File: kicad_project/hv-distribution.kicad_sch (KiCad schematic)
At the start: 33 parts

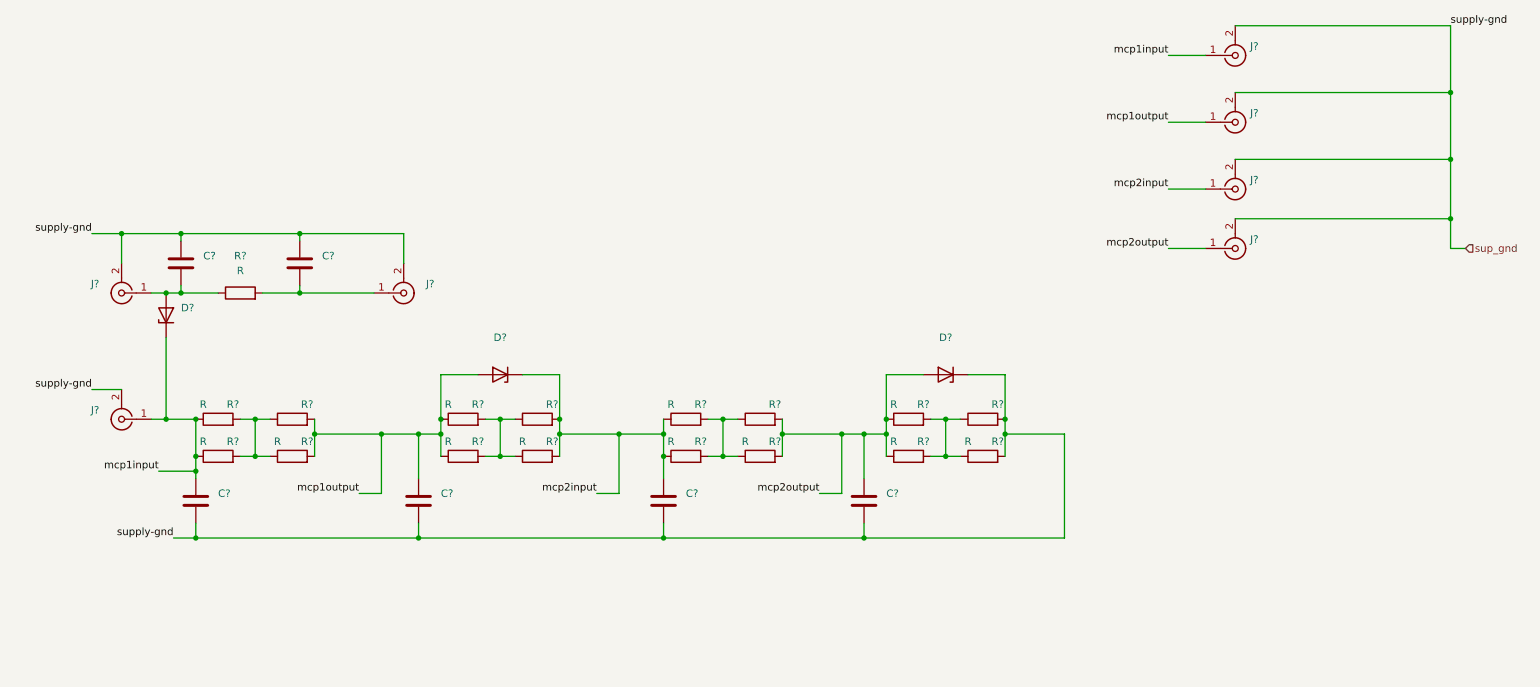
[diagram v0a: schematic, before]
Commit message: Schematic done for HV-circuit. Would like to merge before making layout changes, as some layout changes have been made on other branch and I'm not sure how it will be handled in git
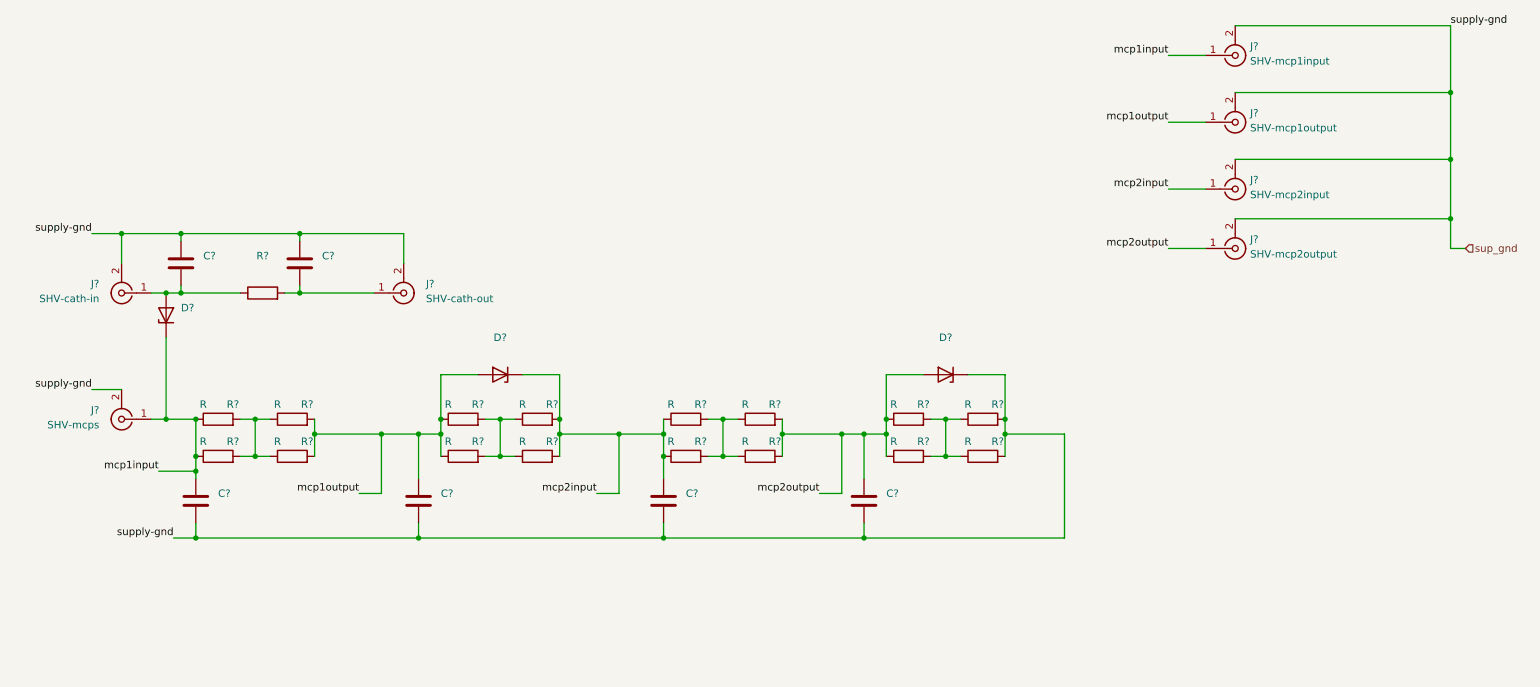
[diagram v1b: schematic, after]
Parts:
- J?: value (none) -> SHV-mcps; footprint (none) -> MountingHole:MountingHole_2.2mm_M2_Pad
- J?: value (none) -> SHV-cath-in; footprint (none) -> MountingHole:MountingHole_2.2mm_M2_Pad
- J?: value (none) -> SHV-mcp2input; footprint (none) -> MountingHole:MountingHole_2.2mm_M2_Pad
- J?: value (none) -> SHV-mcp2output; footprint (none) -> MountingHole:MountingHole_2.2mm_M2_Pad
- J?: value (none) -> SHV-mcp1output; footprint (none) -> MountingHole:MountingHole_2.2mm_M2_Pad
- J?: value (none) -> SHV-mcp1input; footprint (none) -> MountingHole:MountingHole_2.2mm_M2_Pad
- J?: value (none) -> SHV-cath-out; footprint (none) -> MountingHole:MountingHole_2.2mm_M2_Pad
- R? (x4): value (none) -> R; footprint (none) -> Resistor_THT:R_Axial_DIN0614_L14.3mm_D5.7mm_P20.32mm_Horizontal
- R?: value R -> (none)
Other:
- moved on the sheet: R?
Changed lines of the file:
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@@
     (stroke (width 0) (type default) (color 0 0 0 0))
   )
-  (wire (pts (xy 52.07 83.82) (xy 58.42 83.82))
+  (wire (pts (xy 52.07 83.82) (xy 62.23 83.82))
     (stroke (width 0) (type default) (color 0 0 0 0))
   )
@@
     (stroke (width 0) (type default) (color 0 0 0 0))
   )
+  (wire (pts (xy 69.85 83.82) (xy 72.39 83.82))
+    (stroke (width 0) (type default) (color 0 0 0 0))
+  )
   (wire (pts (xy 182.88 105.41) (xy 182.88 111.76))
     (stroke (width 0) (type default) (color 0 0 0 0))
@@
   )
   (wire (pts (xy 127 107.95) (xy 134.62 107.95))
-    (stroke (width 0) (type default) (color 0 0 0 0))
-  )
-  (wire (pts (xy 66.04 83.82) (xy 72.39 83.82))
     (stroke (width 0) (type default) (color 0 0 0 0))
   )
@@
       (effects (font (size 1.27 1.27)) (justify left))
     )
-    (property "Value" "" (id 1) (at 38.1 106.3867 0)
-      (effects (font (size 1.27 1.27)) (justify left))
-    )
-    (property "Footprint" "" (id 2) (at 41.91 105.41 0)
+    (property "Value" "SHV-mcps" (id 1) (at 38.1 106.3867 0)
+      (effects (font (size 1.27 1.27)) (justify left))
+    )
+    (property "Footprint" "MountingHole:MountingHole_2.2mm_M2_Pad" (id 2) (at 41.91 105.41 0)
       (effects (font (size 1.27 1.27)) hide)
     )
@@
       (effects (font (size 1.27 1.27)) (justify left))
     )
-    (property "Value" "" (id 1) (at 38.1 84.7967 0)
-      (effects (font (size 1.27 1.27)) (justify left))
-    )
-    (property "Footprint" "" (id 2) (at 41.91 83.82 0)
+    (property "Value" "SHV-cath-in" (id 1) (at 38.1 84.7967 0)
+      (effects (font (size 1.27 1.27)) (justify left))
+    )
+    (property "Footprint" "MountingHole:MountingHole_2.2mm_M2_Pad" (id 2) (at 41.91 83.82 0)
       (effects (font (size 1.27 1.27)) hide)
     )
@@
     (in_bom yes) (on_board yes)
     (property "Reference" "R?" (id 0) (at 191.77 102.87 90))
-    (property "Value" "" (id 1) (at 186.69 102.87 90))
-    (property "Footprint" "" (id 2) (at 189.23 107.188 90)
+    (property "Value" "R" (id 1) (at 186.69 102.87 90))
+    (property "Footprint" "Resistor_THT:R_Axial_DIN0614_L14.3mm_D5.7mm_P20.32mm_Horizontal" (id 2) (at 189.23 107.188 90)
       (effects (font (size 1.27 1.27)) hide)
     )
@@
     (in_bom yes) (on_board yes)
     (property "Reference" "R?" (id 0) (at 73.66 102.87 90))
-    (property "Value" "" (id 1) (at 68.58 102.87 90))
-    (property "Footprint" "" (id 2) (at 71.12 107.188 90)
+    (property "Value" "R" (id 1) (at 68.58 102.87 90))
+    (property "Footprint" "Resistor_THT:R_Axial_DIN0614_L14.3mm_D5.7mm_P20.32mm_Horizontal" (id 2) (at 71.12 107.188 90)
       (effects (font (size 1.27 1.27)) hide)
     )
@@
     (in_bom yes) (on_board yes)
     (property "Reference" "R?" (id 0) (at 115.57 102.87 90))
-    (property "Value" "" (id 1) (at 110.49 102.87 90))
-    (property "Footprint" "" (id 2) (at 113.03 107.188 90)
+    (property "Value" "R" (id 1) (at 110.49 102.87 90))
+    (property "Footprint" "Resistor_THT:R_Axial_DIN0614_L14.3mm_D5.7mm_P20.32mm_Horizontal" (id 2) (at 113.03 107.188 90)
       (effects (font (size 1.27 1.27)) hide)
     )
@@
     (in_bom yes) (on_board yes)
     (property "Reference" "R?" (id 0) (at 153.67 102.87 90))
-    (property "Value" "" (id 1) (at 148.59 102.87 90))
-    (property "Footprint" "" (id 2) (at 151.13 107.188 90)
+    (property "Value" "R" (id 1) (at 148.59 102.87 90))
+    (property "Footprint" "Resistor_THT:R_Axial_DIN0614_L14.3mm_D5.7mm_P20.32mm_Horizontal" (id 2) (at 151.13 107.188 90)
       (effects (font (size 1.27 1.27)) hide)
     )
@@
       (effects (font (size 1.27 1.27)) (justify left))
     )
-    (property "Value" "" (id 1) (at 234.95 67.0167 0)
-      (effects (font (size 1.27 1.27)) (justify left))
-    )
-    (property "Footprint" "" (id 2) (at 232.41 66.04 0)
+    (property "Value" "SHV-mcp2input" (id 1) (at 234.95 67.0167 0)
+      (effects (font (size 1.27 1.27)) (justify left))
+    )
+    (property "Footprint" "MountingHole:MountingHole_2.2mm_M2_Pad" (id 2) (at 232.41 66.04 0)
       (effects (font (size 1.27 1.27)) hide)
     )
@@
       (effects (font (size 1.27 1.27)) (justify left))
     )
-    (property "Value" "" (id 1) (at 234.95 77.1767 0)
-      (effects (font (size 1.27 1.27)) (justify left))
-    )
-    (property "Footprint" "" (id 2) (at 232.41 76.2 0)
+    (property "Value" "SHV-mcp2output" (id 1) (at 234.95 77.1767 0)
+      (effects (font (size 1.27 1.27)) (justify left))
+    )
+    (property "Footprint" "MountingHole:MountingHole_2.2mm_M2_Pad" (id 2) (at 232.41 76.2 0)
       (effects (font (size 1.27 1.27)) hide)
     )
@@
     (pin "2")
   )
-  (symbol (lib_id "Device:R") (at 62.23 83.82 90) (unit 1)
-    (in_bom yes) (on_board yes) (fields_autoplaced)
-    (property "Reference" "R?" (id 0) (at 62.23 77.47 90))
-    (property "Value" "R" (id 1) (at 62.23 80.01 90))
-    (property "Footprint" "" (id 2) (at 62.23 85.598 90)
-      (effects (font (size 1.27 1.27)) hide)
-    )
-    (property "Datasheet" "~" (id 3) (at 62.23 83.82 0)
+  (symbol (lib_id "Device:R") (at 66.04 83.82 90) (unit 1)
+    (in_bom yes) (on_board yes) (fields_autoplaced)
+    (property "Reference" "R?" (id 0) (at 66.04 77.47 90))
+    (property "Value" "" (id 1) (at 66.04 80.01 90))
+    (property "Footprint" "" (id 2) (at 66.04 85.598 90)
+      (effects (font (size 1.27 1.27)) hide)
+    )
+    (property "Datasheet" "~" (id 3) (at 66.04 83.82 0)
       (effects (font (size 1.27 1.27)) hide)
     )
@@
       (effects (font (size 1.27 1.27)) (justify left))
     )
-    (property "Value" "" (id 1) (at 234.95 55.5867 0)
-      (effects (font (size 1.27 1.27)) (justify left))
-    )
-    (property "Footprint" "" (id 2) (at 232.41 54.61 0)
+    (property "Value" "SHV-mcp1output" (id 1) (at 234.95 55.5867 0)
+      (effects (font (size 1.27 1.27)) (justify left))
+    )
+    (property "Footprint" "MountingHole:MountingHole_2.2mm_M2_Pad" (id 2) (at 232.41 54.61 0)
       (effects (font (size 1.27 1.27)) hide)
     )
@@
       (effects (font (size 1.27 1.27)) (justify left))
     )
-    (property "Value" "" (id 1) (at 234.95 44.1567 0)
-      (effects (font (size 1.27 1.27)) (justify left))
-    )
-    (property "Footprint" "" (id 2) (at 232.41 43.18 0)
+    (property "Value" "SHV-mcp1input" (id 1) (at 234.95 44.1567 0)
+      (effects (font (size 1.27 1.27)) (justify left))
+    )
+    (property "Footprint" "MountingHole:MountingHole_2.2mm_M2_Pad" (id 2) (at 232.41 43.18 0)
       (effects (font (size 1.27 1.27)) hide)
     )
@@
       (effects (font (size 1.27 1.27)) (justify left))
     )
-    (property "Value" "" (id 1) (at 93.98 84.7967 0)
-      (effects (font (size 1.27 1.27)) (justify left))
-    )
-    (property "Footprint" "" (id 2) (at 90.17 83.82 0)
-      (effects (font (size 1.27 1.27)) hide)
-    )
+    (property "Value" "SHV-cath-out" (id 1) (at 93.98 84.7967 0)
+      (effects (font (size 1.27 1.27)) (justify left))
+    )
+    (property "Footprint" "MountingHole:MountingHole_2.2mm_M2_Pad" (id 2) (at 90.17 83.82 0)
+      (effects (font (size 1.27 1.27)) hide)
+    )

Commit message: First draft layout of HV circuit. Things to refine: (1) ground return pads / mounting holes for gnd return. (2) Idea of how the high voltage inputs/outputs actually hook up to the LAPPD and incoming cables. (3) UL796 standard has 1.6kV/mm rating on distances between conductors. Is this tolerance actually OK, considering the present layout of gnd pour. (4) Do all of the components clear mechanical constraints of the LAPPD and Ultem frame, i.e. we wont have a solder mound where the detector or frame needs to be flush.
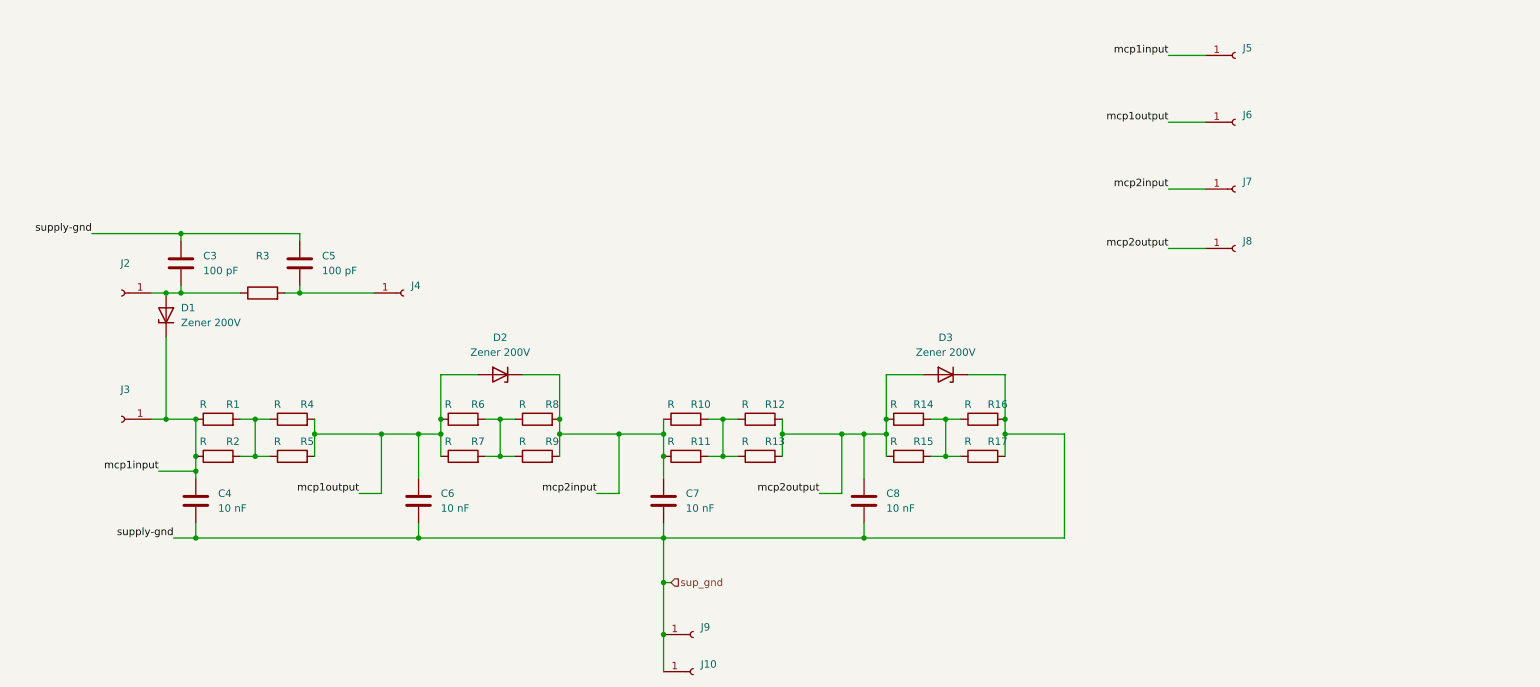
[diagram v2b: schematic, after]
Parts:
- removed J?: SHV-mcps, MountingHole:MountingHole_2.2mm_M2_Pad, symbol Connector:Conn_Coaxial
- removed J?: SHV-cath-in, MountingHole:MountingHole_2.2mm_M2_Pad, symbol Connector:Conn_Coaxial
- removed J?: SHV-mcp2input, MountingHole:MountingHole_2.2mm_M2_Pad, symbol Connector:Conn_Coaxial
- removed J?: SHV-mcp2output, MountingHole:MountingHole_2.2mm_M2_Pad, symbol Connector:Conn_Coaxial
- removed J?: SHV-mcp1output, MountingHole:MountingHole_2.2mm_M2_Pad, symbol Connector:Conn_Coaxial
- removed J?: SHV-mcp1input, MountingHole:MountingHole_2.2mm_M2_Pad, symbol Connector:Conn_Coaxial
- removed J?: SHV-cath-out, MountingHole:MountingHole_2.2mm_M2_Pad, symbol Connector:Conn_Coaxial
- added J10, J2, J4, J5, J6, J7, J8, J9: (no value), MountingHole:MountingHole_2.2mm_M2_Pad, symbol Connector:Conn_01x01_Female
- added J3: (no value), symbol Connector:Conn_01x01_Female
- C3, C5: renamed from C?; value (none) -> 100 pF; footprint (none) -> Capacitor_THT:CP_Radial_D8.0mm_P5.00mm
- C4, C6, C7, C8: renamed from C?; value (none) -> 10 nF; footprint (none) -> Capacitor_THT:CP_Radial_D8.0mm_P5.00mm
- D1, D2, D3: renamed from D?; value (none) -> Zener 200V; footprint (none) -> Diode_THT:D_A-405_P12.70mm_Horizontal
- gave numbers to parts that had none: 17
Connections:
- net mcp1input: now also C4.2, J3.1 (Pin_1), J5.1 (Pin_1); no longer C4.1
- net mcp1output: now also C6.2, J6.1 (Pin_1); no longer C6.1
- net mcp2input: now also C7.2, J7.1 (Pin_1); no longer C7.1
- net mcp2output: now also C8.2, J8.1 (Pin_1); no longer C8.1
- net sup_gnd: now also C4.1, C6.1, C7.1, C8.1, J10.1 (Pin_1), J9.1 (Pin_1); no longer C4.2, C6.2, C7.2, C8.2
- net at C3.2, D1.2 (A), R3.1: now also J2.1 (Pin_1)
- net at C5.2, R3.2: now also J4.1 (Pin_1)
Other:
- moved on the sheet: C4, C6, C7, C8
